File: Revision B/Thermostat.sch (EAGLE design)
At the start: 22 parts, among them K1 G5LE, K2 G5LE, K3 G5LE

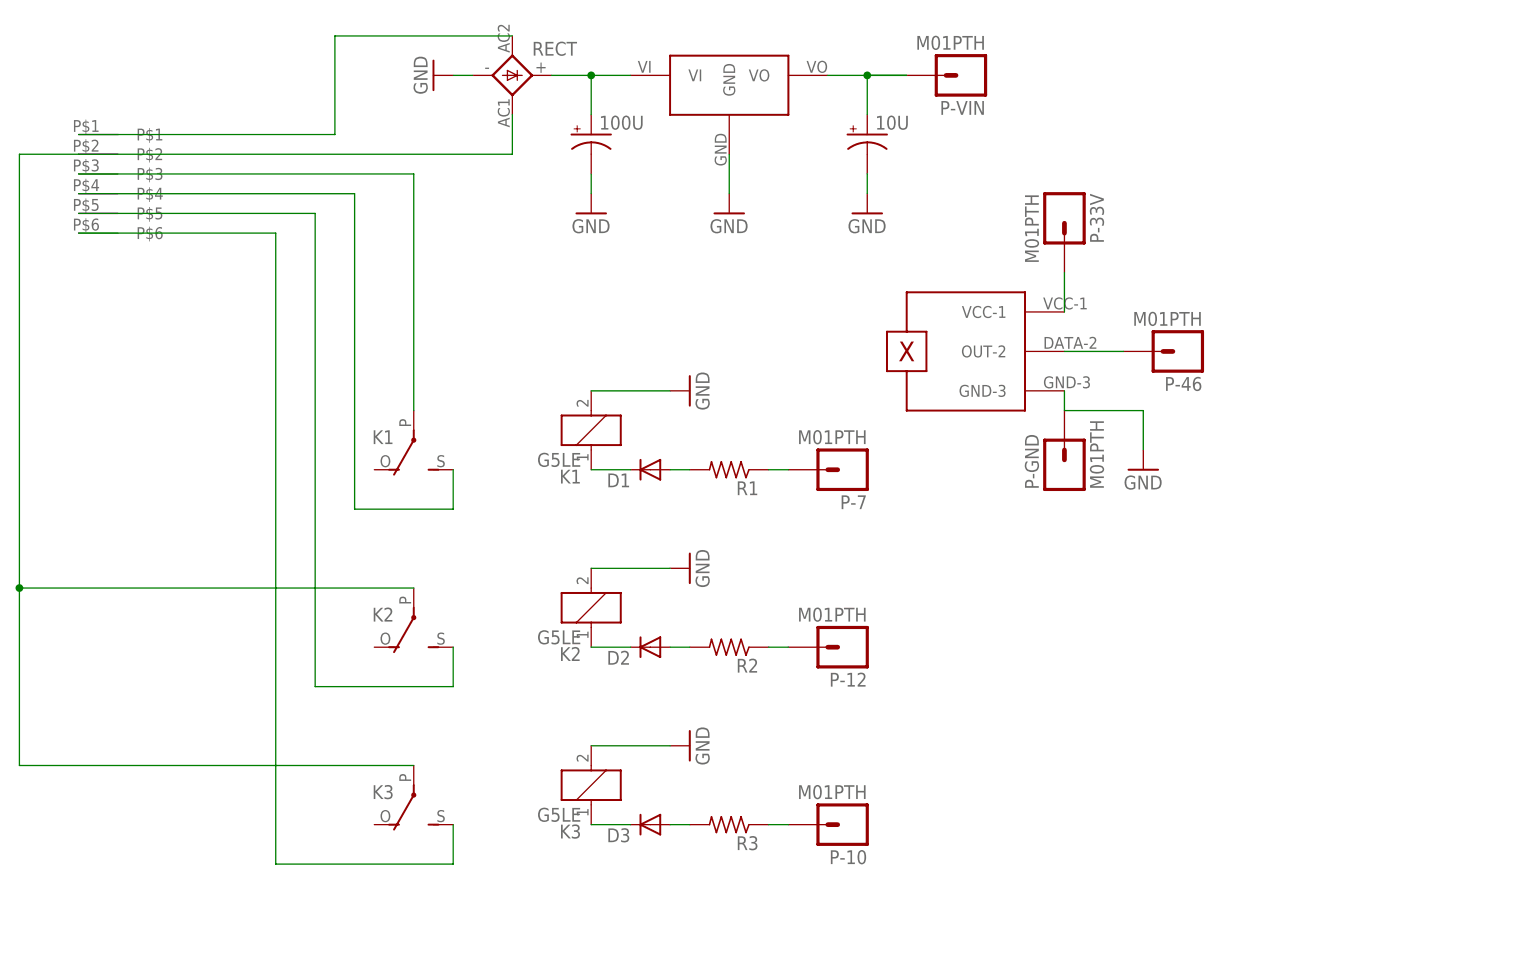
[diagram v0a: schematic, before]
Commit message: Added Transistors
The IOIO can only supply 20ma from the digital pins, so I added
transistors to feed 5v and switched to the 5v relays.
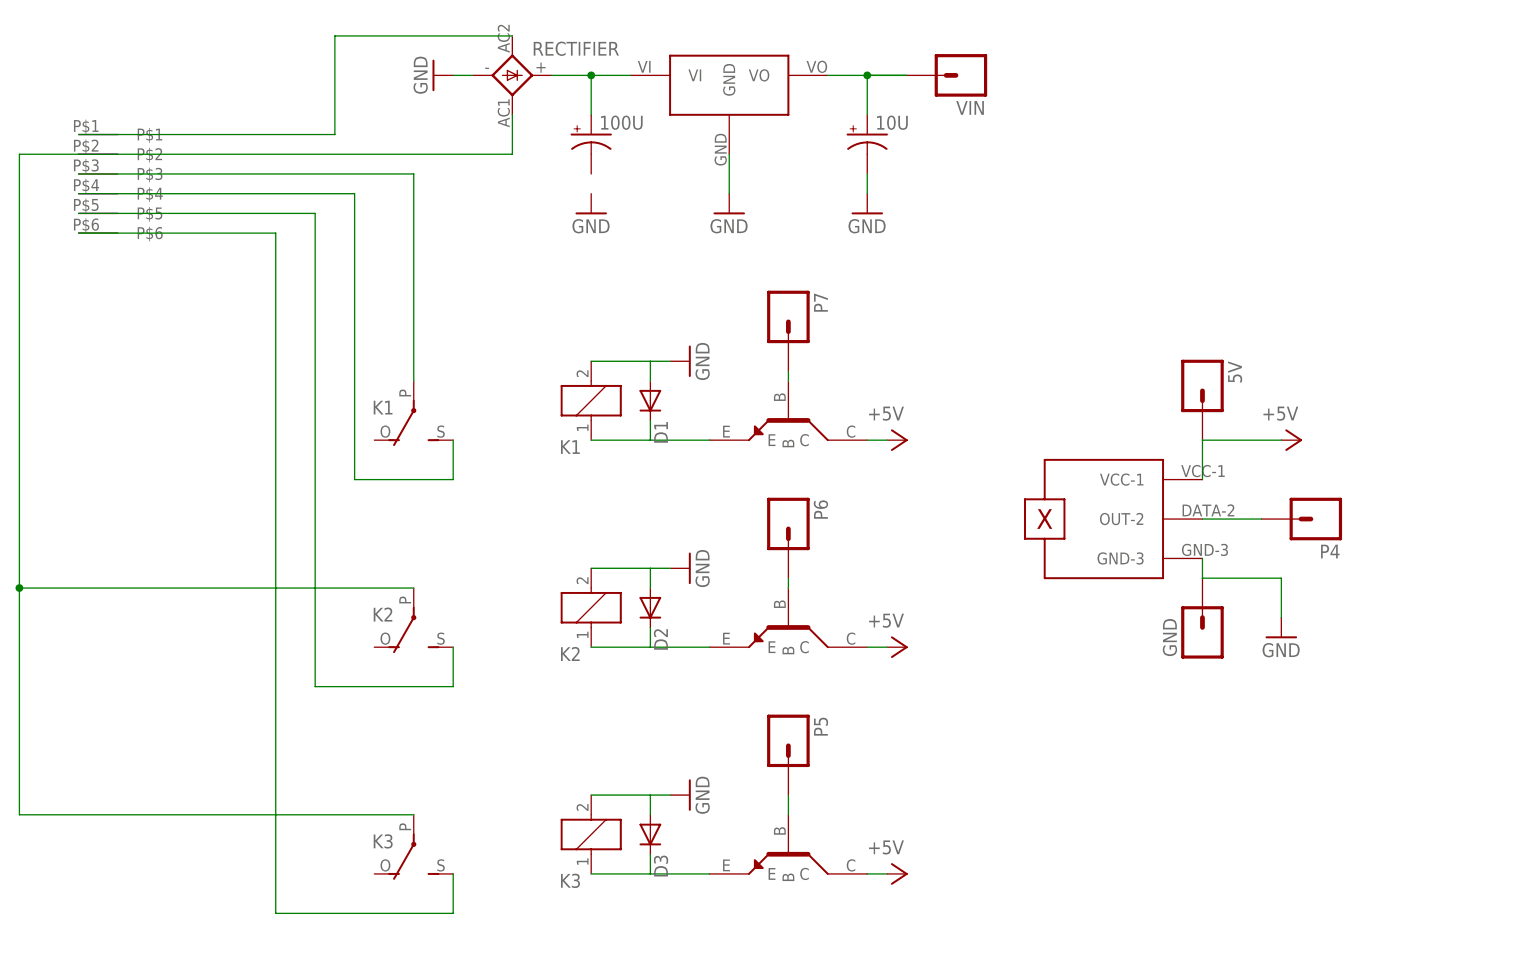
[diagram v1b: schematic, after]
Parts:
- removed P-10, P-12, P-33V, P-46, P-7, P-GND: M01PTH, SparkFun-Connectors:M01PTH
- removed R1, R2, R3: (no value), resistor:R-US_0204/2V
- added 5V, GND, P4, P5, P6, P7: M01PTH, SparkFun-Connectors:M01PTH
- added U$4, U$5, U$6: TRANSISTOR, android-thermostat:TRANSISTOR
- renumbered P-VIN to VIN, RECT to RECTIFIER
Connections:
- removed net GND: 100U.-, 10U.-, K11.2, K21.2, K31.2, P-GND.1, RECTIFIER.-, U$1.GND-3, U$2.GND
- removed net N$17: P-7.1, R1.1
- removed net N$27: P-12.1, R2.1
- removed net N$9: D1.C, K11.1
- new net +5V: 5V.1, U$1.VCC-1, U$4.C, U$5.C, U$6.C
- net N$11: now also D2.C, K21.1, U$5.E; no longer P-46.1, U$1.OUT-2
- net N$16: now also D3.C, K31.1, U$6.E; no longer D1.A, R1.2
- net N$2: now also 10U.-, D1.A, D2.A, D3.A, GND.1, K11.2, K21.2, K31.2, RECTIFIER.-, U$1.GND-3, U$2.GND; no longer P-10.1, R3.1
- net N$3: now also P7.1, U$4.B; no longer D3.A, R3.2
- net N$4: now also P4.1, U$1.OUT-2; no longer D3.C, K31.1
- net N$6: now also P6.1, U$5.B; no longer D2.C, K21.1
- net N$7: now also P5.1, U$6.B; no longer D2.A, R2.2
- net N$8: now also D1.C, K11.1, U$4.E; no longer P-33V.1, U$1.VCC-1
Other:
- moved on the sheet: D1, D2, D3, K1, K3

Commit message: Finished Board Layout with Transistors
Changed the transistor symbol.
Changed wires to routes
Verified against design rules
Added top and bottom silk text
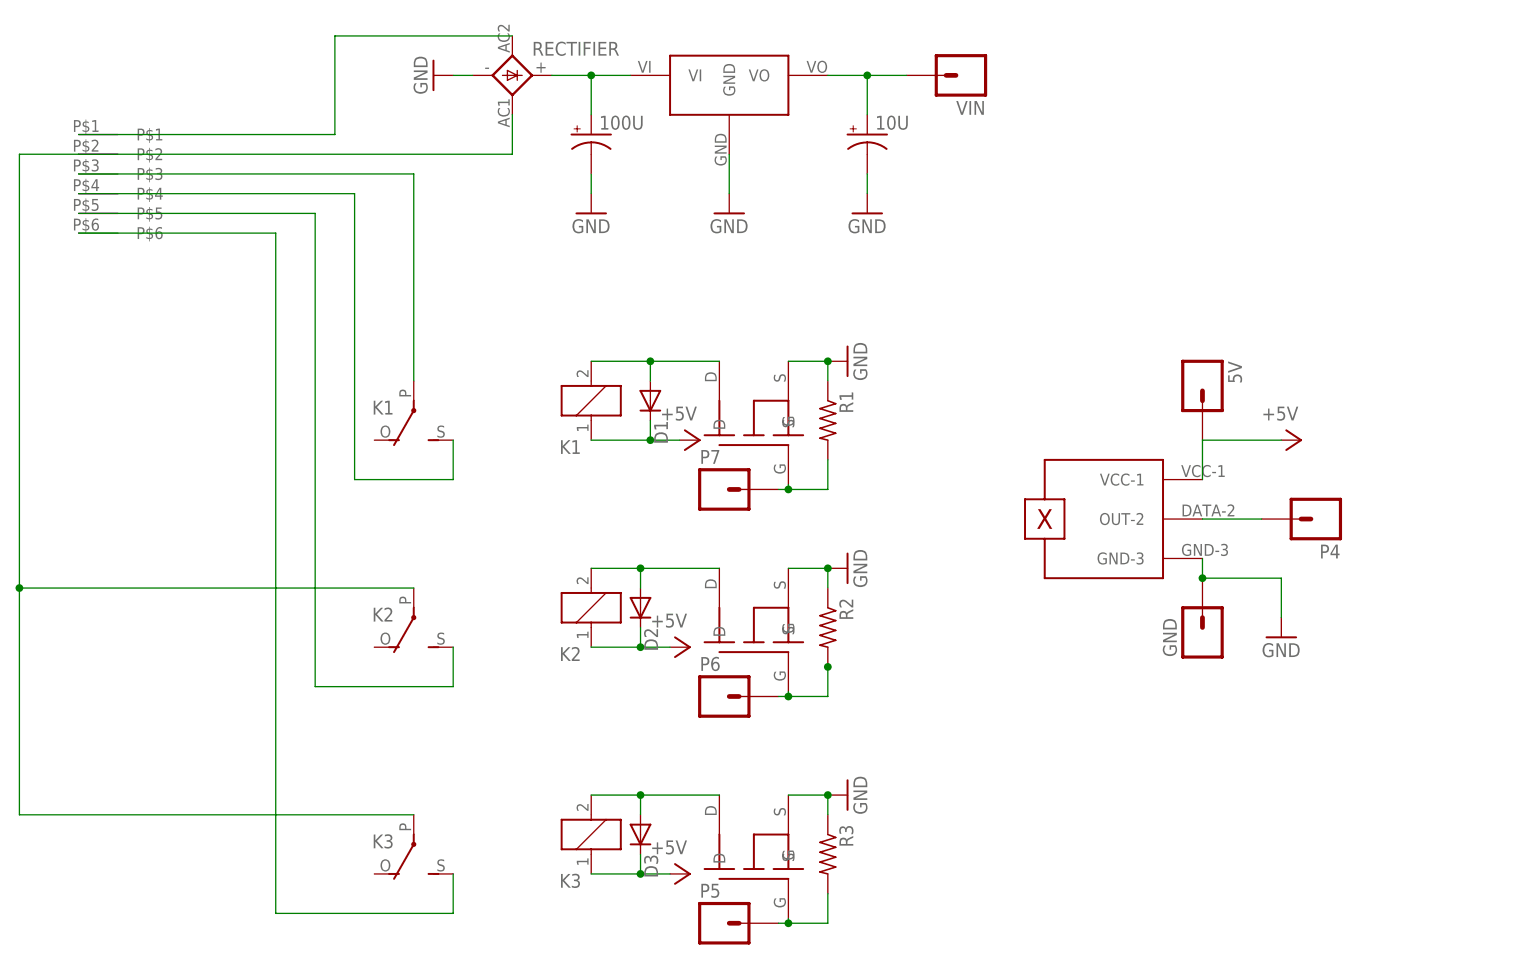
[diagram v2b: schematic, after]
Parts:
- removed U$4, U$5, U$6: TRANSISTOR, android-thermostat:TRANSISTOR
- added R1, R2, R3: (no value), rcl:R-US_0204/7
- added T1, T2, T3: MOSFET, android-thermostat:MOSFET
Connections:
- removed net N$11: D2.C, K21.1, U$5.E
- removed net N$8 (its old number): D1.C, K11.1, U$4.E
- new net GND: 100U.-, 10U.-, GND.1, R1.1, R2.1, R3.1, RECTIFIER.-, T1.S, T2.S, T3.S, U$1.GND-3, U$2.GND
- new net N$17: P5.1, R3.2, T3.G
- new net N$18: D3.A, K31.2, T3.D
- net +5V: now also D1.C, D2.C, D3.C, K11.1, K21.1, K31.1; no longer 5V.1, U$1.VCC-1, U$4.C, U$5.C, U$6.C
- net N$16: now also 5V.1, U$1.VCC-1; no longer D3.C, K31.1, U$6.E
- net N$2: now also P6.1, R2.2, T2.G; no longer 10U.-, D1.A, D2.A, D3.A, GND.1, K11.2, K21.2, K31.2, RECTIFIER.-, U$1.GND-3, U$2.GND
- net N$3: now also D2.A, K21.2, T2.D; no longer P7.1, U$4.B
- net N$6: now also P7.1, R1.2, T1.G; no longer P6.1, U$5.B
- net N$7: now also D1.A, K11.2, T1.D; no longer P5.1, U$6.B
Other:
- moved on the sheet: D2, D3, P5, P6, P7

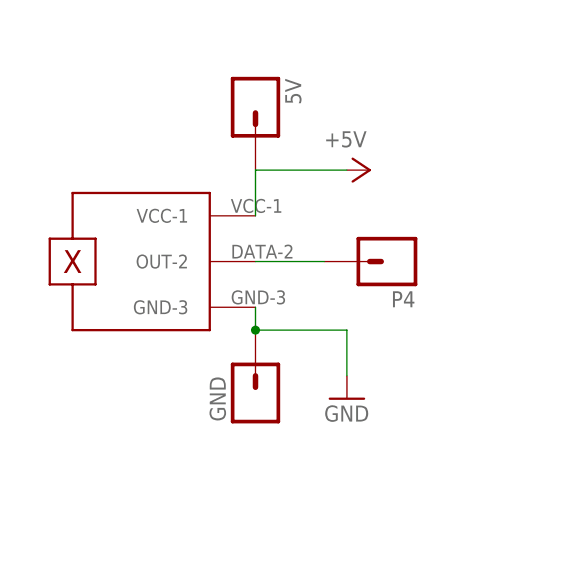
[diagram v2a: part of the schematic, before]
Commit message: Added Temperature Sensor Capacitor
Added a capacitor to pin 4 to smooth out the voltage reading from the
temperature sensor.  I still need to calculate exactly what size that
capacitor should be.
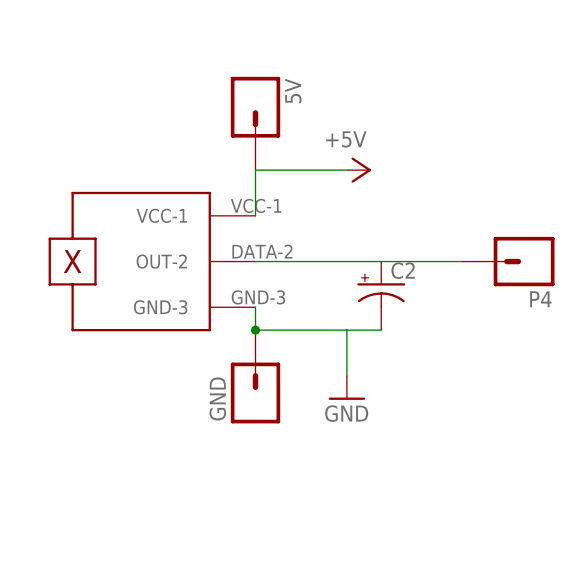
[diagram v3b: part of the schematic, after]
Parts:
- added C2: (no value), rcl:CPOL-USE2-5
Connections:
- net GND: now also C2.-
- net N$4: now also C2.+
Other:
- moved on the sheet: P4
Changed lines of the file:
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@@
 <part name="T2" library="android-thermostat" deviceset="MOSFET" device=""/>
 <part name="T1" library="android-thermostat" deviceset="MOSFET" device=""/>
+<part name="C2" library="rcl" deviceset="CPOL-US" device="E2-5"/>
 </parts>
 <sheets>
@@
 <instance part="5V" gate="G$1" x="111.76" y="54.61" rot="R270"/>
 <instance part="GND" gate="G$1" x="111.76" y="21.59" rot="R90"/>
-<instance part="P4" gate="G$1" x="127" y="36.83" rot="R180"/>
+<instance part="P4" gate="G$1" x="142.24" y="36.83" rot="R180"/>
 <instance part="P6" gate="G$1" x="49.53" y="13.97"/>
 <instance part="P5" gate="G$1" x="49.53" y="-15.24"/>
@@
 <instance part="T2" gate="G$1" x="54.61" y="21.59" rot="R90"/>
 <instance part="T1" gate="G$1" x="54.61" y="48.26" rot="R90"/>
+<instance part="C2" gate="G$1" x="125.73" y="34.29"/>
 </instances>
 <busses>
@@
 <wire x1="121.92" y1="29.21" x2="121.92" y2="24.13" width="0.3048" layer="91"/>
 <junction x="111.76" y="29.21"/>
+<pinref part="C2" gate="G$1" pin="-"/>
+<wire x1="121.92" y1="29.21" x2="125.73" y2="29.21" width="0.3048" layer="91"/>
 </segment>
 <segment>
@@
 <pinref part="GND5" gate="1" pin="GND"/>
 <wire x1="17.78" y1="93.98" x2="15.24" y2="93.98" width="0.3048" layer="91"/>
-</segment>
-</net>
-<net name="N$4" class="0">
-<segment>
-<pinref part="P4" gate="G$1" pin="1"/>
-<pinref part="U$1" gate="G$1" pin="OUT-2"/>
-<wire x1="119.38" y1="36.83" x2="111.76" y2="36.83" width="0.3048" layer="91"/>
 </segment>
 </net>
@@
 </segment>
 </net>
+<net name="N$4" class="0">
+<segment>
+<pinref part="U$1" gate="G$1" pin="OUT-2"/>
+<pinref part="C2" gate="G$1" pin="+"/>
+<wire x1="111.76" y1="36.83" x2="125.73" y2="36.83" width="0.3048" layer="91"/>
+<pinref part="P4" gate="G$1" pin="1"/>
+<wire x1="125.73" y1="36.83" x2="134.62" y2="36.83" width="0.3048" layer="91"/>
+</segment>
+</net>

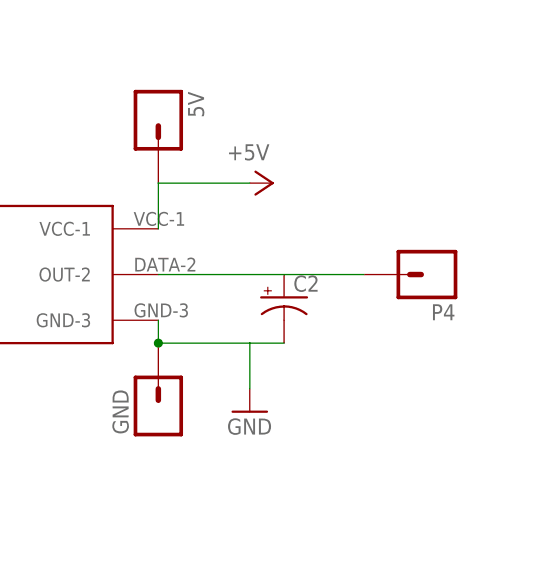
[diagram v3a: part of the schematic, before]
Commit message: Added Temperature Sensor Resistor
Added a 150k resistor to the temperature sensor to drop the amps to 5uA,
below the 7uA output of the temperature sensor, in order to allow the
capacitor to charge.
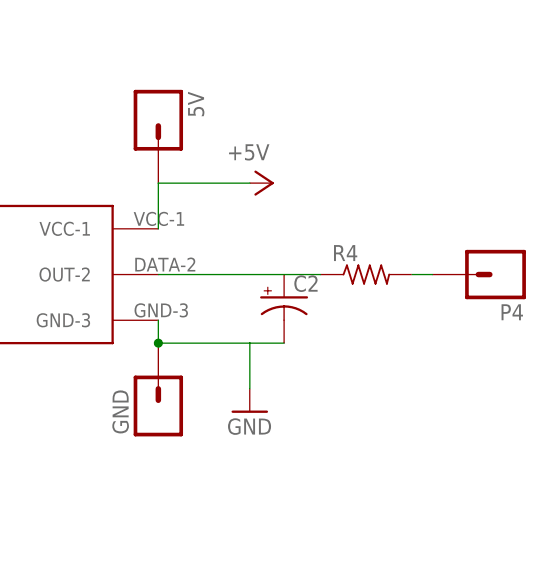
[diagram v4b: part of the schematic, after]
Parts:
- added R4: (no value), rcl:R-US_0204/5
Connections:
- new net N$5: P4.1, R4.2
- net N$4: now also R4.1; no longer P4.1
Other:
- moved on the sheet: P4
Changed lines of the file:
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@@
 <part name="T1" library="android-thermostat" deviceset="MOSFET" device=""/>
 <part name="C2" library="rcl" deviceset="CPOL-US" device="E2-5"/>
+<part name="R4" library="rcl" deviceset="R-US_" device="0204/5"/>
 </parts>
 <sheets>
@@
 <instance part="5V" gate="G$1" x="111.76" y="54.61" rot="R270"/>
 <instance part="GND" gate="G$1" x="111.76" y="21.59" rot="R90"/>
-<instance part="P4" gate="G$1" x="142.24" y="36.83" rot="R180"/>
+<instance part="P4" gate="G$1" x="149.86" y="36.83" rot="R180"/>
 <instance part="P6" gate="G$1" x="49.53" y="13.97"/>
 <instance part="P5" gate="G$1" x="49.53" y="-15.24"/>
@@
 <instance part="T1" gate="G$1" x="54.61" y="48.26" rot="R90"/>
 <instance part="C2" gate="G$1" x="125.73" y="34.29"/>
+<instance part="R4" gate="G$1" x="134.874" y="36.83"/>
 </instances>
 <busses>
@@
 <pinref part="C2" gate="G$1" pin="+"/>
 <wire x1="111.76" y1="36.83" x2="125.73" y2="36.83" width="0.3048" layer="91"/>
+<pinref part="R4" gate="G$1" pin="1"/>
+<wire x1="129.794" y1="36.83" x2="125.73" y2="36.83" width="0.3048" layer="91"/>
+</segment>
+</net>
+<net name="N$5" class="0">
+<segment>
+<pinref part="R4" gate="G$1" pin="2"/>
 <pinref part="P4" gate="G$1" pin="1"/>
-<wire x1="125.73" y1="36.83" x2="134.62" y2="36.83" width="0.3048" layer="91"/>
-</segment>
-</net>
+<wire x1="139.954" y1="36.83" x2="142.24" y2="36.83" width="0.3048" layer="91"/>
+</segment>
+</net>
